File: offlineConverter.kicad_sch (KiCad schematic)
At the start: 72 parts, among them IC1 NCP12510ASN65T1G, IC2 SFH6156-3, J5 640445-2, Q1 STD3NK80ZT4, Q6 BC847, U2 AZ431LANTR

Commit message: Rev. 1.0.0 production data
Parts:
- renumbered F1 to F3, J5 to ST2
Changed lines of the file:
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@@
 		(polyline
 			(pts
-				(xy 165.1 110.49) (xy 165.1 77.47) (xy 24.13 77.47) (xy 24.13 109.22) (xy 36.83 109.22) (xy 36.83 85.09)
-				(xy 87.63 85.09) (xy 87.63 110.49) (xy 92.71 110.49)
+				(xy 53.34 29.21) (xy 53.34 73.66) (xy 180.34 73.66) (xy 180.34 54.61) (xy 223.52 54.61) (xy 223.52 29.21)
 			)
 			(stroke
@@
 		(polyline
 			(pts
-				(xy 53.34 29.21) (xy 53.34 73.66) (xy 180.34 73.66) (xy 180.34 54.61) (xy 223.52 54.61) (xy 223.52 29.21)
+				(xy 165.1 110.49) (xy 165.1 77.47) (xy 24.13 77.47) (xy 24.13 109.22) (xy 36.83 109.22) (xy 36.83 85.09)
+				(xy 87.63 85.09) (xy 87.63 110.49) (xy 92.71 110.49)
 			)
 			(stroke
@@
 		(on_board yes)
 		(dnp no)
-		(property "Reference" "J5"
+		(property "Reference" "ST2"
 			(at 276.86 138.43 0)
 			(effects
@@
 			(project "OSLUV"
 				(path "/c6e900e0-9399-44f0-8089-9dd7b8ffe54c/a8d7965e-5268-4c95-93ca-40f8dbbf325c"
-					(reference "J5")
+					(reference "ST2")
 					(unit 1)
 				)
@@
 		(dnp no)
 		(fields_autoplaced yes)
-		(property "Reference" "F1"
+		(property "Reference" "F3"
 			(at 53.34 38.1 0)
 			(effects
@@
 			(project "OSLUV"
 				(path "/c6e900e0-9399-44f0-8089-9dd7b8ffe54c/a8d7965e-5268-4c95-93ca-40f8dbbf325c"
-					(reference "F1")
+					(reference "F3")
 					(unit 1)
 				)

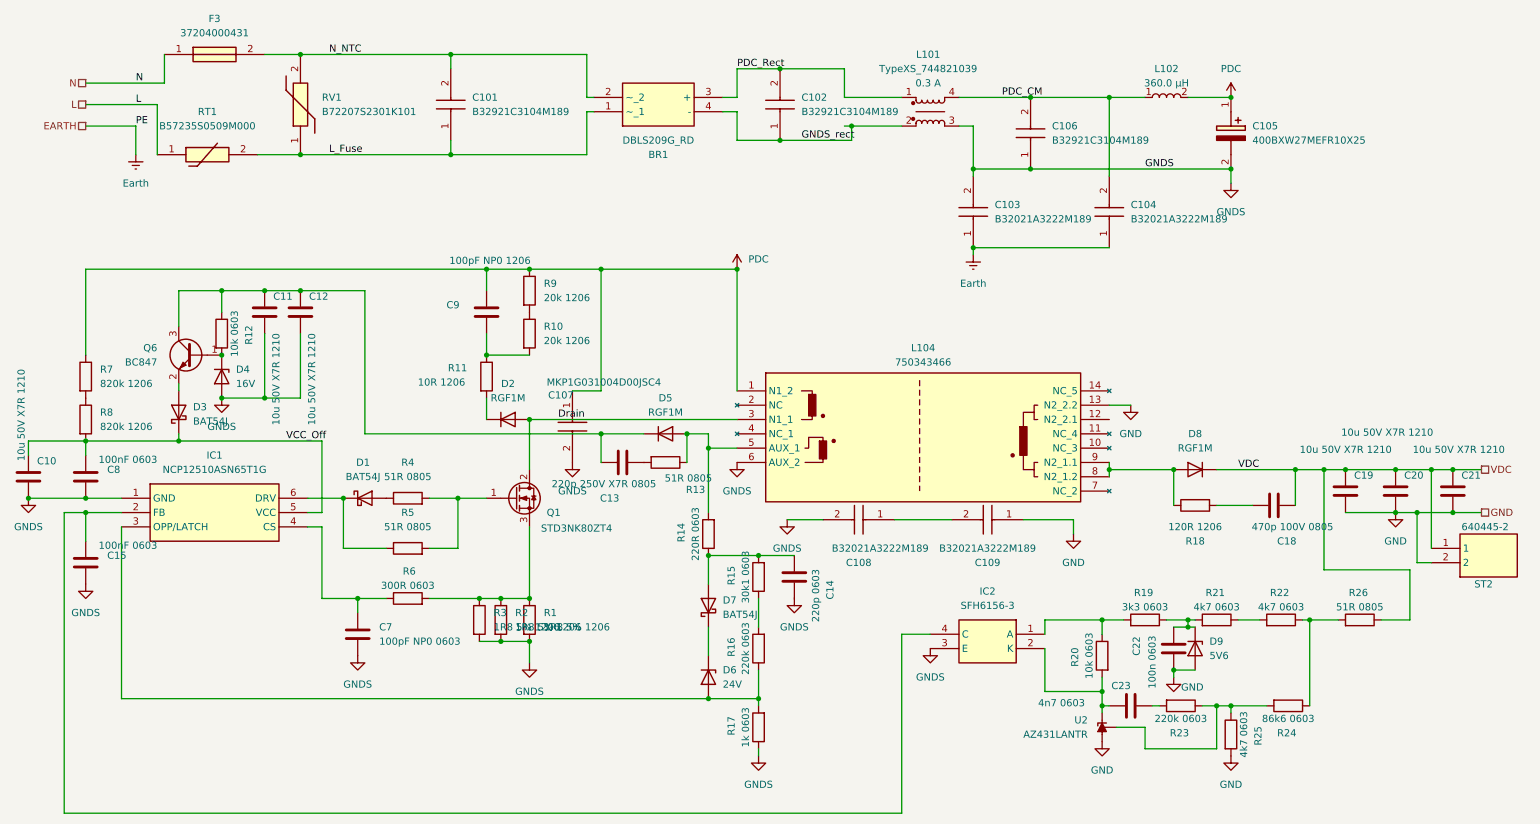
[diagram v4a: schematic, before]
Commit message: Rev 1.0.0 corrected component values
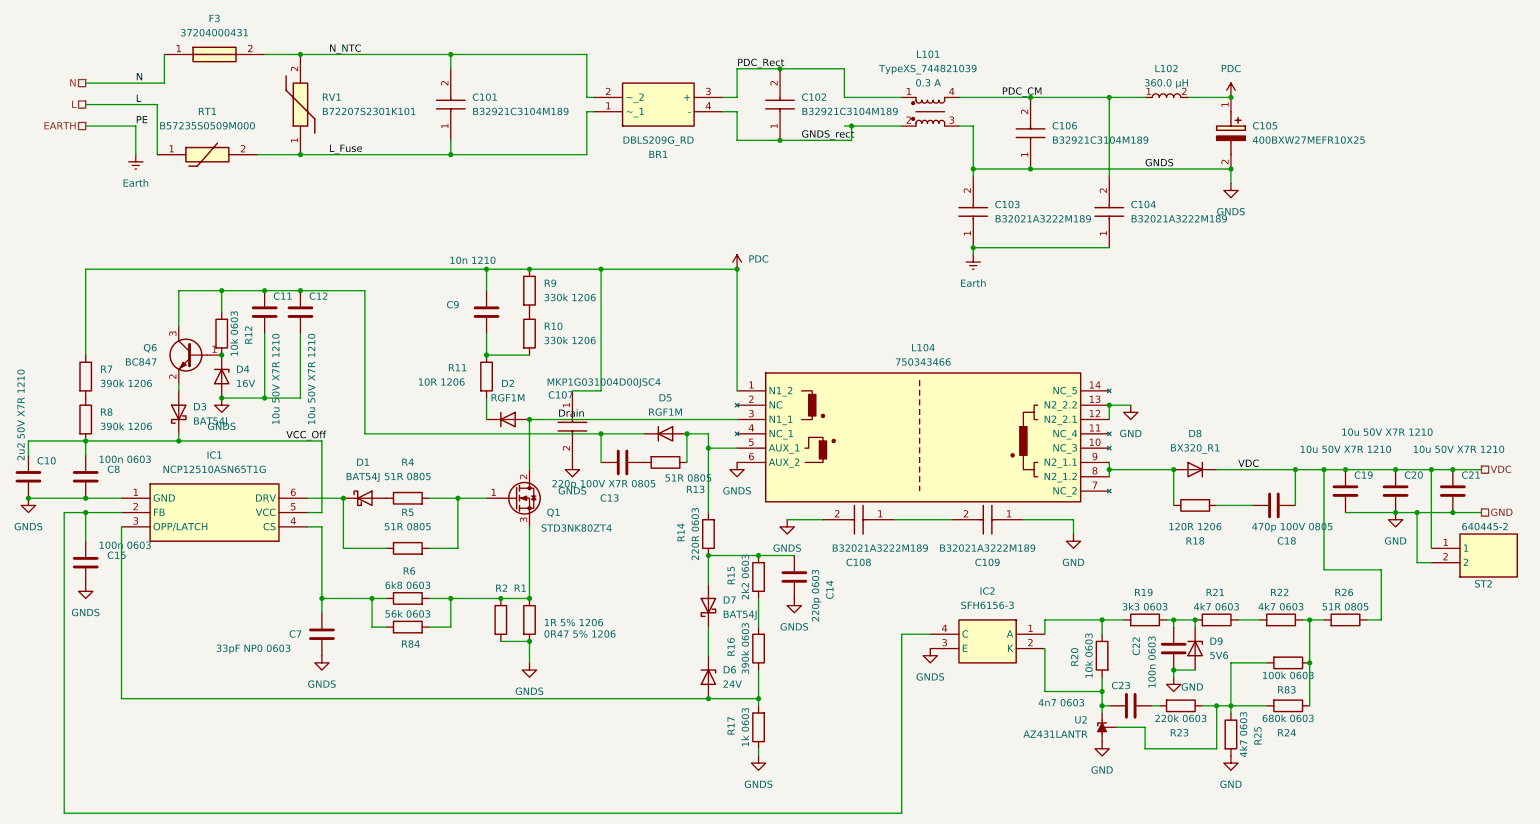
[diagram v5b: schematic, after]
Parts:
- removed R3: 1R8 5% 1206, Resistor_SMD:R_1206_3216Metric, symbol Device:R
- added R83: 100k 0603, Resistor_SMD:R_0603_1608Metric, symbol Device:R
- added R84: 56k 0603, Resistor_SMD:R_0603_1608Metric, symbol Device:R
- C10: value 10u 50V X7R 1210 -> 2u2 50V X7R 1210
- C13: value 220p 250V X7R 0805 -> 220p 100V X7R 0805
- C15, C8: value 100nF 0603 -> 100n 0603
- C7: value 100pF NP0 0603 -> 33pF NP0 0603
- C9: value 100pF NP0 1206 -> 10n 1210; footprint Capacitor_SMD:C_1206_3216Metric -> Capacitor_SMD:C_1210_3225Metric
- D8: value RGF1M -> BX320_R1
- R1: value 1R8 5% 1206 -> 0R47 5% 1206
- R10, R9: value 20k 1206 -> 330k 1206
- R15: value 30k1 0603 -> 2k2 0603
- R16: value 220k 0603 -> 390k 0603
- R2: value 1R8 5% 1206 -> 1R 5% 1206
- R24: value 86k6 0603 -> 680k 0603
- R6: value 300R 0603 -> 6k8 0603
- R7, R8: value 820k 1206 -> 390k 1206
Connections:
- net GND: now also L104.12 (N2_2.1)
- net at C7.1, IC1.4 (CS), R6.1: now also R84.1
- net at R23.1, R24.2, R25.1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: now also R83.2
- net at R22.1, R24.1, R26.2: now also R83.1
- net at Q1.3 (S), R1.1, R2.1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: now also R84.2
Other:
- moved on the sheet: C7, R26
